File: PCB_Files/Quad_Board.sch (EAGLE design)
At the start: 38 parts

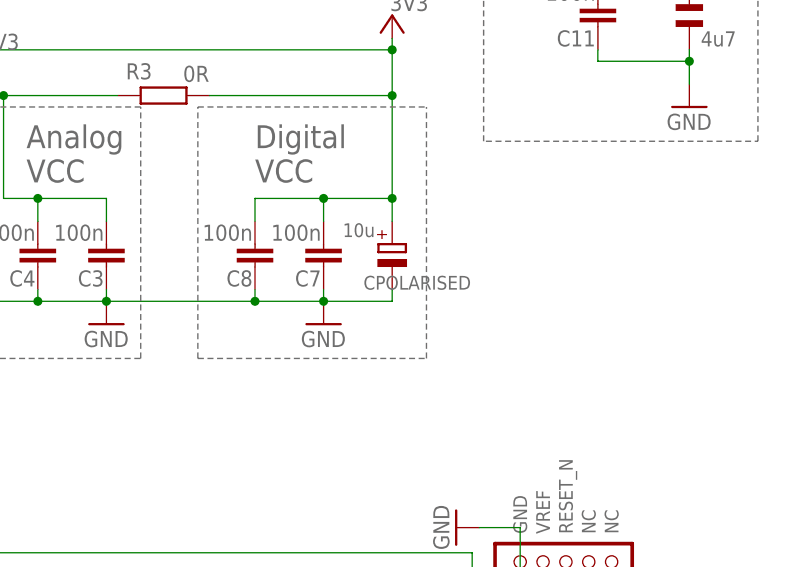
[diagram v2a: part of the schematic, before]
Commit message: Adding more silscreen info
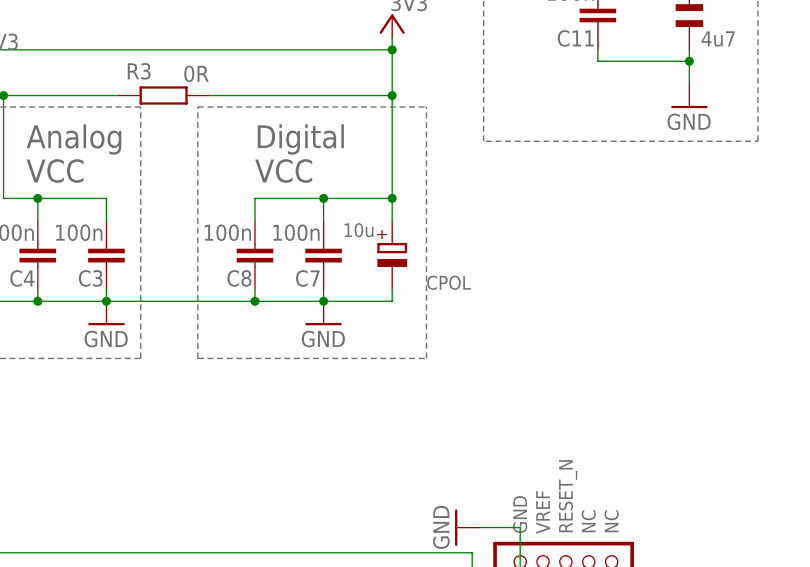
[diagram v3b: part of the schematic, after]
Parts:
- renumbered CPOLARISED to CPOL
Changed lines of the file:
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@@
 <part name="C7" library="rcl" deviceset="C-EU" device="C0805" value="100n"/>
 <part name="C8" library="rcl" deviceset="C-EU" device="C0805" value="100n"/>
-<part name="CPOLARISED" library="rcl" deviceset="CPOL-EU" device="A/3216-18R" value="10u"/>
+<part name="CPOL" library="rcl" deviceset="CPOL-EU" device="A/3216-18R" value="10u"/>
 <part name="R3" library="rcl" deviceset="R-EU_" device="RM0402" value="0R"/>
 <part name="GND44" library="supply1" deviceset="GND" device=""/>
@@
 <attribute name="VALUE" x="-184.404" y="103.759" size="1.778" layer="96" rot="R180"/>
 </instance>
-<instance part="CPOLARISED" gate="G$1" x="-168.91" y="101.6" smashed="yes">
+<instance part="CPOL" gate="G$1" x="-168.91" y="101.6" smashed="yes">
 <attribute name="NAME" x="-160.147" y="98.0694" size="1.524" layer="95" rot="R180"/>
 <attribute name="VALUE" x="-170.815" y="103.9114" size="1.524" layer="96" rot="R180"/>
@@
 <junction x="-184.15" y="95.25"/>
 <wire x1="-176.53" y1="95.25" x2="-168.91" y2="95.25" width="0.1524" layer="91"/>
-<pinref part="CPOLARISED" gate="G$1" pin="-"/>
+<pinref part="CPOL" gate="G$1" pin="-"/>
 <wire x1="-168.91" y1="96.52" x2="-168.91" y2="95.25" width="0.1524" layer="91"/>
 <wire x1="-200.66" y1="95.25" x2="-184.15" y2="95.25" width="0.1524" layer="91"/>
@@
 <segment>
 <wire x1="-189.23" y1="118.11" x2="-168.91" y2="118.11" width="0.1524" layer="91"/>
-<pinref part="CPOLARISED" gate="G$1" pin="+"/>
+<pinref part="CPOL" gate="G$1" pin="+"/>
 <wire x1="-168.91" y1="118.11" x2="-168.91" y2="106.68" width="0.1524" layer="91"/>
 <pinref part="R3" gate="G$1" pin="1"/>

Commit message: P+Completed PCB barring reference IC ppoints
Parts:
- C1, C2: value (none) -> 1u
- R7: value (none) -> 100k
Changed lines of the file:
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@@
 <part name="ULTRA4" library="pinhead" deviceset="PINHD-1X4" device=""/>
 <part name="5V_PDB" library="pinhead" deviceset="PINHD-1X2" device=""/>
-<part name="C1" library="rcl" deviceset="C-EU" device="C0805"/>
-<part name="C2" library="rcl" deviceset="C-EU" device="C0805"/>
+<part name="C1" library="rcl" deviceset="C-EU" device="C0805" value="1u"/>
+<part name="C2" library="rcl" deviceset="C-EU" device="C0805" value="1u"/>
 <part name="GND50" library="supply1" deviceset="GND" device=""/>
 <part name="C3" library="rcl" deviceset="C-EU" device="C0805" value="100n"/>
@@
 <part name="FRAME1" library="frames" deviceset="FRAME_D_L" device=""/>
 <part name="U$1" library="TXS0102-bi-directional-translator" deviceset="TXS0102" device=""/>
-<part name="R7" library="resistor" deviceset="R-EU_" device="M1206"/>
+<part name="R7" library="resistor" deviceset="R-EU_" device="M1206" value="100k"/>
 <part name="GND2" library="SparkFun-Aesthetics" deviceset="GND" device=""/>
 <part name="GND3" library="SparkFun-Aesthetics" deviceset="GND" device=""/>

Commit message: New PCB design
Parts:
- removed MINIJTAG: (no value), kblom:JTAG-AVR-IDC
- added C13: 1n, rcl:C-EUC0805
- added JTAG: EXTERNAL_DEBUG_CON, MSP-EXP432:EXTERNAL_DEBUG_CON
- added LED2, POWER_LED: (no value), eagle-ltspice:LED_E
- added R10, R9: 1k, resistor:R-EU_M0805
- added R2: 47k, rcl:R-EU_R1206
- added R8: 1k, rcl:R-EU_R1206
- added U$4: TACTILE-SWITCH-PTH, GeekAmmo:TACTILE-SWITCH-PTH
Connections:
- removed net !RST: MINIJTAG.RESET_N, MSP432P401R.RSTN/NMI
- removed net 5V: LEVEL_TRANSLATOR1.VCCB, LEVEL_TRANSLATOR_2.VCCB, LEVEL_TRANSLATOR_3.VCCB, U$1.P$3, U$3.P$2
- removed net TCK_SWCLK: MINIJTAG.TCK, MSP432P401R.SWCLKTCK
- removed net TDI: MINIJTAG.TDI, MSP432P401R.PJ.4/TDI/ADC14CLK
- removed net TDO_SWO: MINIJTAG.TDO, MSP432P401R.PJ.5/TDO/SWO
- removed net TMS_SWDIO: MINIJTAG.TMS, MSP432P401R.SWDIOTMS
- new net DEBUG_RESET: C13.1, JTAG.10, MSP432P401R.RSTN/NMI, R2.1, U$4.3, U$4.4
- new net DEBUG_SWCLK: JTAG.4, MSP432P401R.SWCLKTCK
- new net DEBUG_SWDIO: JTAG.2, MSP432P401R.SWDIOTMS
- new net DEBUG_SWO: JTAG.6, MSP432P401R.PJ.5/TDO/SWO
- new net DEBUG_TDI: JTAG.8, MSP432P401R.PJ.4/TDI/ADC14CLK
- new net LED1_SIGNAL: MSP432P401R.P8.3/TA3CLK/A22, R9.2
- new net LED2_SIGNAL: MSP432P401R.P8.4/A21, R10.2
- new net N$14: JTAG.1, R8.2
- new net N$5: POWER_LED.A, R9.1
- new net N$6: LED2.A, R10.1
- net 3V3: now also R2.2, R8.1, U$1.P$3, U$2.OUT_5, U$3.P$2; no longer R1.1, R7.1, U$1.P$6, U$1.P$7, U$3.P$6, U$3.P$7
- net 5VDC: now also LEVEL_TRANSLATOR1.VCCB, LEVEL_TRANSLATOR_2.VCCB, LEVEL_TRANSLATOR_3.VCCB, R1.1, R7.1, U$1.P$6, U$1.P$7, U$3.P$6, U$3.P$7
- net A1: now also U$1.P$4; no longer U$1.P$5
- net A2: now also U$1.P$5; no longer U$1.P$4
- net B1: now also U$1.P$1; no longer U$1.P$8
- net B2: now also U$1.P$8; no longer U$1.P$1
- net GND: now also C13.2, JTAG.3, JTAG.5, JTAG.7, JTAG.9, LED2.C, POWER_LED.C, U$4.1, U$4.2; no longer MINIJTAG.GND
- net P2.2_RX: now also U$3.P$4; no longer U$3.P$5
- net VBAT_TX: now also U$3.P$5; no longer U$3.P$4
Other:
- note added: "External Debugger Connector for MSP432P401R device Bypass XDS-ET, use S101"
- note added: "RESET"
